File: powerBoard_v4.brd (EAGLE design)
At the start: 23.2 x 34.9 mm, 25 parts, among them U1 TLE2426CD

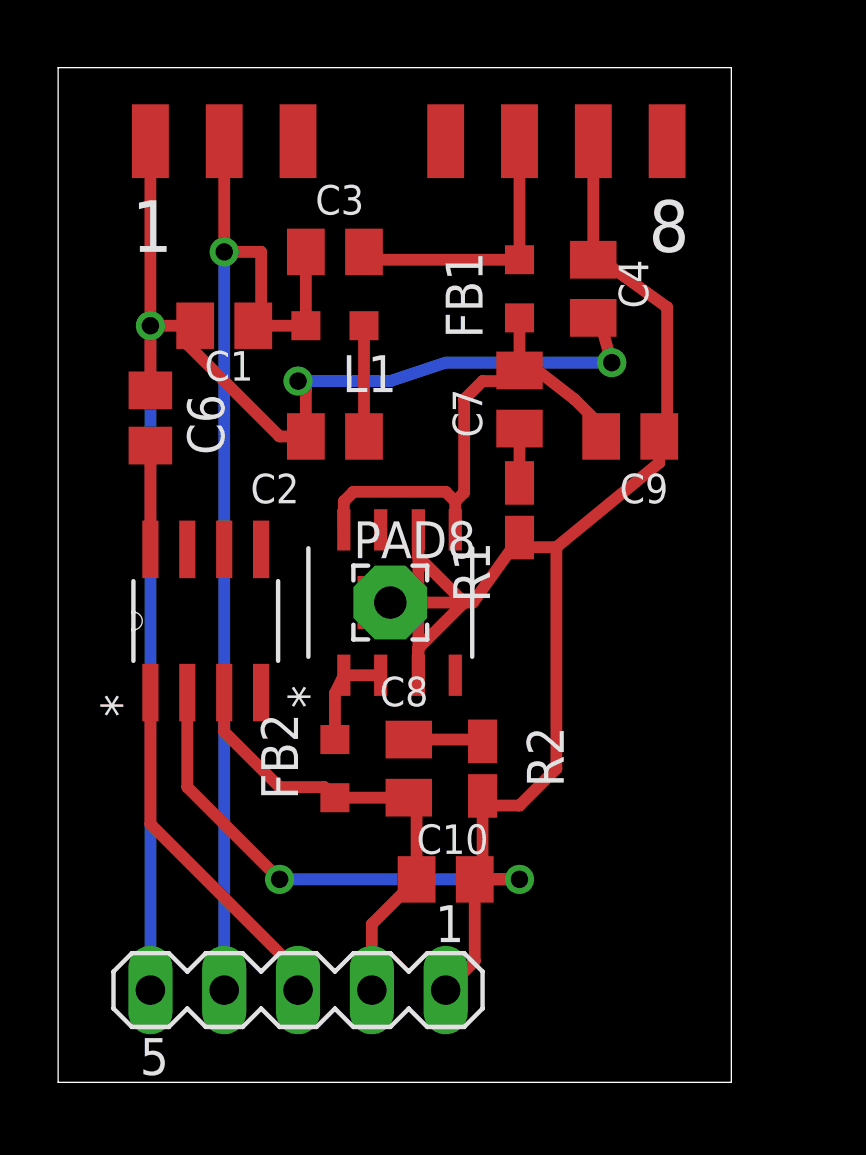
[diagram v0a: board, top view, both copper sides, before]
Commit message: updated power board designs: v2 uses low current 2.5v reference, v3 uses 10v rail and 5v ref both with simple linear regulators. Added breakout board to go from DB37 to BNC
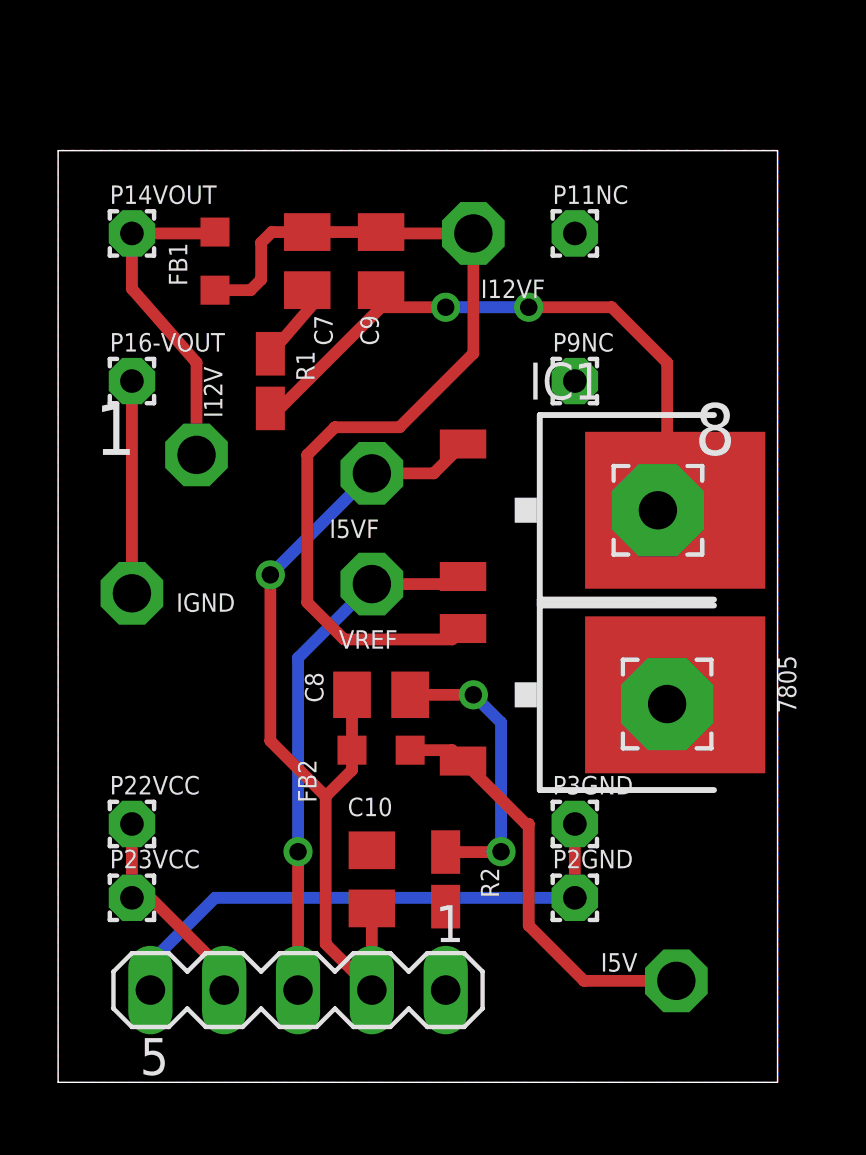
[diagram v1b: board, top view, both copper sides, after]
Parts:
- removed C1, C2: 10uf, rcl:C0805K
- removed C3, C4: 470pf, rcl:C0805K
- removed C6: 1uF, rcl:C0805
- removed L1: 12uH, resistor:L2012C
- removed PAD2, PAD3, PAD4, PAD5, PAD6, PAD7: (no value), wirepad:SMD1,27-2,54
- removed U$1: ADP7105-REGULATOR, tuckerLib:ADP7105-REGULATOR
- removed U1: TLE2426CD, Texas Instruments_By_element14_Batch_1:SOIC127P600X175-8N
- added 7805: 7806DT, linear:TO252
- added I12V, I12VF, I5V, I5VF, IGND, VREF: PTR1PAD1-13, testpad:P1-13
- added IC1: 7805DT, linear:TO252
- added P11NC, P14VOUT, P16-VOUT, P22VCC, P23VCC, P2GND, P3GND, P9NC: WIREPAD1,6/0,8, wirepad:1,6/0,8
- PAD1: value (none) -> WIREPAD3,17/1,3; device wirepad:SMD1,27-2,54 -> wirepad:3,17/1,3
- PAD8: value (none) -> WIREPAD3,17/1,3; device wirepad:2,54/1,1 -> wirepad:3,17/1,3
- moved PAD1 21.6 mm to (20.6, 19.7)
- moved FB1 10.5 mm to (5.40, 28.3)
- moved C9 10.5 mm to (11.1, 28.3), turned to 270 degrees
- moved PAD8 10.1 mm to (21.0, 13.0)
- moved R1 9.66 mm to (7.30, 24.1)
- moved C7 8.72 mm to (8.57, 28.3)
- moved R2 4.02 mm to (13.3, 6.99)
- moved C8 2.71 mm to (11.1, 13.3), turned to 0 degrees
- moved C10 2.54 mm to (10.8, 6.99), turned to 90 degrees
- moved FB2 1.71 mm to (11.1, 11.4), turned to 180 degrees
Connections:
- removed net N$1: C2.1, L1.2
- removed net N$2: C6.1, U1.8
- removed net NC0: PAD3.1
- removed net NC1: PAD4.1
- removed net NC2: PAD7.1
- removed net NC3: U$1.4
- removed net PG: U$1.7
- net GND: now also P2GND.1, P3GND.1; no longer C1.2, C2.2, C4.2, C6.2, PAD1.1
- net VCC: now also P22VCC.1, P23VCC.1; no longer C1.1, C3.2, L1.1, PAD2.1
- net VREF: now also IC1.2, VREF.TP; no longer U1.1
- net VS1+: now also I12V.TP, P14VOUT.1; no longer C3.1, PAD5.1
- net VS1-: now also 7805.3, IC1.3, IGND.TP, P16-VOUT.1, PAD1.1; no longer C4.1, PAD6.1, U$1.3, U$1.6, U$1.9, U1.2
- net VS1F+: now also 7805.1, I12VF.TP; no longer U$1.5, U$1.8
- net VS2+: now also 7805.2, I5V.TP; no longer U$1.1, U$1.2
- net VS2F+: now also I5VF.TP, IC1.1; no longer U1.3
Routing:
- net VS1-: track 72.4 -> 29.0 mm
- net GND: track 53.7 -> 19.0 mm, vias 3 -> 0
- net VCC: track 37.6 -> 7.40 mm, vias 1 -> 0
- net VS1F+: track 17.9 -> 32.9 mm
- net VS2F+: track 16.4 -> 30.9 mm, vias 0 -> 1
- net VS2+: track 3.55 -> 14.5 mm
- net N$3: track 2.56 -> 9.88 mm, vias 0 -> 2
- net VREF: track 12.3 -> 18.3 mm, vias 0 -> 1
- net N$1: track 4.19 -> 0.00 mm
- net N$2: track 3.57 -> 0.00 mm
- net VS1+: track 9.54 -> 11.3 mm
- net N$4: track 1.87 -> 2.92 mm
- added copper zone on layer 16, net GND
- added copper zone on layer 1, net VS1-
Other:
- board size 23.2 x 34.9 mm -> 24.8 x 32.1 mm
- board text added: "10V@200mA"
- board text added: "5V@200mA"
- board text added: "Dec 2016"
- board text added: "V3"
- board text added: "input: 9-18V@500mA"
- board text removed: "2.5V@300mA"
- board text removed: "5V@300mA"
- board text removed: "Aug 2016"
- board text removed: "V1"
- board text removed: "input 9-18V@1A"

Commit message: updated V4 powerboard to actually include switchmode pads. Added BOM for backplane and daughter card
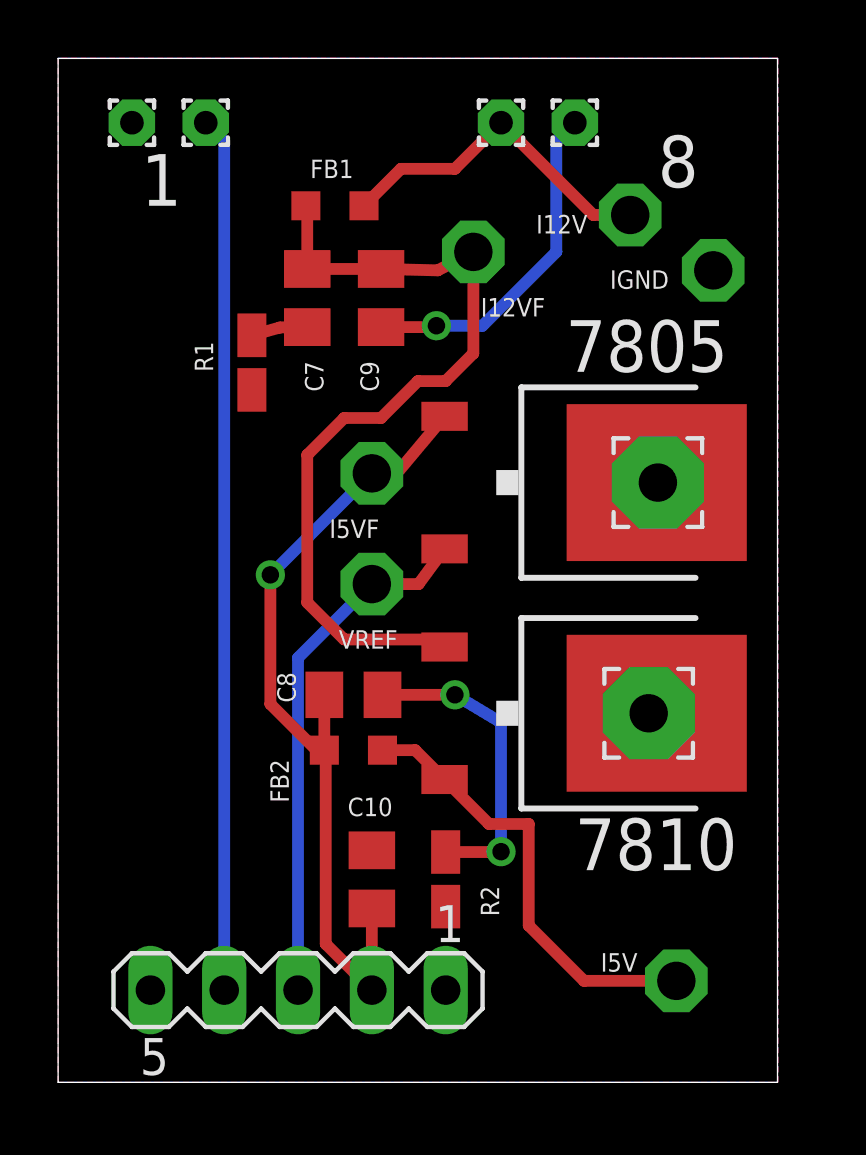
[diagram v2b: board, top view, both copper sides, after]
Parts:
- removed IC1: 7805DT, linear:TO252
- removed P11NC, P23VCC, P3GND, P9NC: WIREPAD1,6/0,8, wirepad:1,6/0,8
- added 7810: 7806DT, linear:TO252
- 7805: value 7806DT -> 7805DT
- moved P2GND 30.7 mm to (2.54, 33.0)
- moved P22VCC 24.3 mm to (5.08, 33.0)
- moved IGND 22.9 mm to (22.5, 27.9)
- moved P16-VOUT 17.6 mm to (17.8, 33.0)
- moved I12V 17.1 mm to (19.7, 29.8)
- moved P14VOUT 13.3 mm to (15.2, 33.0)
- moved 7805 7.33 mm to (18.1, 20.6)
- moved FB1 4.55 mm to (9.53, 30.2), turned to 180 degrees
- moved C7 1.27 mm to (8.57, 27.0)
- moved C9 1.27 mm to (11.1, 27.0)
- moved C8 0.95 mm to (10.2, 13.3)
- moved FB2 0.95 mm to (10.2, 11.4)
- moved PAD1 0.95 mm to (20.6, 20.6)
- moved R1 0.90 mm to (6.67, 24.8)
- moved PAD8 0.71 mm to (20.3, 12.7)
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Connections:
- net GND: no longer P3GND.1
- net VCC: no longer P23VCC.1
- net VREF: now also 7805.2; no longer IC1.2
- net VS1-: now also 7810.3; no longer IC1.3
- net VS1F+: now also 7810.1; no longer 7805.1
- net VS2+: now also 7810.2; no longer 7805.2
- net VS2F+: now also 7805.1; no longer IC1.1
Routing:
- net VCC: track 7.40 -> 30.1 mm
- net GND: track 19.0 -> 0.00 mm
- net VS1-: track 29.0 -> 11.8 mm, vias 2 -> 1
- net VS1F+: track 32.9 -> 29.7 mm
- net VS2F+: track 30.9 -> 29.1 mm
- net N$4: track 2.92 -> 1.94 mm
- net VS2+: track 14.5 -> 15.4 mm
- net N$3: track 9.88 -> 10.7 mm
- net VREF: track 18.3 -> 18.1 mm, vias 1 -> 0
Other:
- board size 24.8 x 32.1 mm -> 24.8 x 35.2 mm
- board text added: "7805"
- board text added: "7810"

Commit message: minor labeling and component placement updates. most significant is correcting part position on powerboard so 22uF bypass cap actually connects to ground.
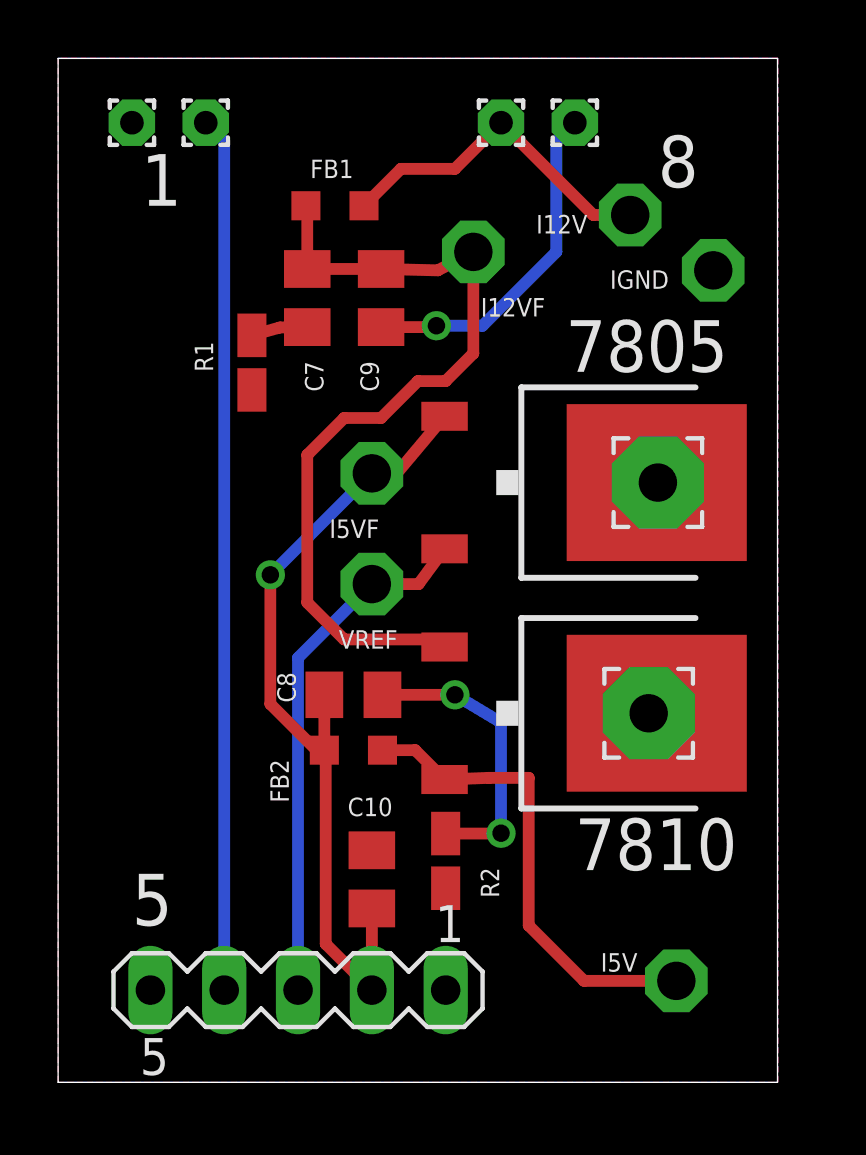
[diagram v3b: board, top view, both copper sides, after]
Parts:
- moved R2 0.63 mm to (13.3, 7.62)
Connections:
- net VS1-: no longer R2.1
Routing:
- net VS2+: track 15.4 -> 16.4 mm
- net N$3: track 10.7 -> 10.1 mm
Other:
- board text added: "5"
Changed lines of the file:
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@@
 <text x="2.8575" y="30.1625" size="1.778" layer="25">1</text>
 <text x="20.6375" y="30.7975" size="1.778" layer="25">8</text>
-<text x="8.89" y="12.3825" size="1.016" layer="26" rot="MR0">10V@200mA</text>
-<text x="9.2075" y="10.4775" size="1.016" layer="26" rot="MR0">5V@200mA</text>
+<text x="9.2075" y="14.2875" size="1.016" layer="26" rot="MR0">10V@200mA</text>
+<text x="9.2075" y="12.3825" size="1.016" layer="26" rot="MR0">5V@200mA</text>
 <text x="23.1775" y="25.4" size="1.27" layer="26" rot="MR0">DC-DC isolator</text>
 <text x="23.1775" y="23.495" size="1.27" layer="26" rot="MR0">and voltage</text>
 <text x="22.86" y="21.59" size="1.27" layer="26" rot="MR0">regulator</text>
-<text x="22.86" y="12.3825" size="1.27" layer="26" rot="MR0">input:
+<text x="22.86" y="14.2875" size="1.27" layer="26" rot="MR0">input:
 9-18V@500mA</text>
-<text x="8.255" y="14.2875" size="1.27" layer="26" rot="MR0">output:</text>
+<text x="9.2075" y="15.875" size="1.27" layer="26" rot="MR0">output:</text>
 <text x="5.08" y="23.8125" size="1.778" layer="26" rot="MR0">V3</text>
 <text x="18.415" y="18.415" size="1.27" layer="26" rot="MR0">Dec 2016</text>
-<text x="14.605" y="1.27" size="1.778" layer="27">1</text>
+<text x="15.5575" y="0.9525" size="1.778" layer="27">1</text>
 <text x="17.4625" y="24.4475" size="1.778" layer="25">7805</text>
 <text x="17.78" y="7.3025" size="1.778" layer="25">7810</text>
+<text x="2.54" y="5.3975" size="1.778" layer="25">5</text>
 </plain>
 <attributes>
@@
 <attribute name="NAME" x="11.5075" y="9.795" size="0.635" layer="25" rot="R180"/>
 </element>
-<element name="R2" library="resistor" package="R2012W" value="0.33" x="13.335" y="6.985" smashed="yes" rot="R90">
-<attribute name="NAME" x="15.1765" y="5.715" size="0.635" layer="25" rot="R90"/>
+<element name="R2" library="resistor" package="R2012W" value="0.33" x="13.335" y="7.62" smashed="yes" rot="R90">
+<attribute name="NAME" x="15.1765" y="6.35" size="0.635" layer="25" rot="R90"/>
 </element>
 <element name="PAD8" library="wirepad" package="3,17/1,3" value="WIREPAD3,17/1,3" x="20.32" y="12.7" smashed="yes">
@@
 <wire x1="13.2975" y1="10.42" x2="12.2875" y2="11.43" width="0.4064" layer="1"/>
 <wire x1="12.2875" y1="11.43" x2="11.16" y2="11.43" width="0.4064" layer="1"/>
-<wire x1="13.2975" y1="10.42" x2="14.8275" y2="8.89" width="0.4064" layer="1"/>
-<wire x1="14.8275" y1="8.89" x2="16.1925" y2="8.89" width="0.4064" layer="1"/>
-<wire x1="16.1925" y1="8.89" x2="16.1925" y2="5.3975" width="0.4064" layer="1"/>
+<wire x1="13.2975" y1="10.42" x2="14.8275" y2="10.4775" width="0.4064" layer="1"/>
+<wire x1="14.8275" y1="10.4775" x2="16.1925" y2="10.4775" width="0.4064" layer="1"/>
+<wire x1="16.1925" y1="10.4775" x2="16.1925" y2="5.3975" width="0.4064" layer="1"/>
 <wire x1="16.1925" y1="5.3975" x2="18.0975" y2="3.4925" width="0.4064" layer="1"/>
 <wire x1="18.0975" y1="3.4925" x2="21.2725" y2="3.4925" width="0.4064" layer="1"/>
@@
 <contactref element="IGND" pad="TP"/>
 <contactref element="7810" pad="3"/>
-<contactref element="R2" pad="1"/>
-<contactref element="C10" pad="2"/>
-<contactref element="PAD8" pad="1"/>
 <polygon width="0.4064" layer="1" isolate="0.4064">
 <vertex x="0" y="0"/>
@@
 <wire x1="13.0175" y1="26.035" x2="12.97" y2="25.9875" width="0.4064" layer="1"/>
 <wire x1="12.97" y1="25.9875" x2="11.1125" y2="25.9875" width="0.4064" layer="1"/>
+<contactref element="C10" pad="2"/>
+<contactref element="PAD8" pad="1"/>
 </signal>
 <signal name="VS2F+">
@@
 <via x="13.6525" y="13.335" extent="1-16" drill="0.6" shape="square"/>
 <wire x1="13.6525" y1="13.335" x2="15.24" y2="12.3825" width="0.4064" layer="16"/>
-<wire x1="15.24" y1="12.3825" x2="15.24" y2="7.9375" width="0.4064" layer="16"/>
-<via x="15.24" y="7.9375" extent="1-16" drill="0.6" shape="square"/>
-<wire x1="15.24" y1="7.9375" x2="15.2275" y2="7.925" width="0.4064" layer="1"/>
-<wire x1="15.2275" y1="7.925" x2="13.335" y2="7.925" width="0.4064" layer="1"/>
+<wire x1="15.24" y1="12.3825" x2="15.24" y2="8.5725" width="0.4064" layer="16"/>
+<via x="15.24" y="8.5725" extent="1-16" drill="0.6" shape="square"/>
+<wire x1="15.24" y1="8.5725" x2="15.2275" y2="8.56" width="0.4064" layer="1"/>
+<wire x1="15.2275" y1="8.56" x2="13.335" y2="8.56" width="0.4064" layer="1"/>
 </signal>
 </signals>
